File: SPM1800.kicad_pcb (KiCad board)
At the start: 2 copper layers, 314.3 x 83.3 mm, 140 parts, among them J1 Conn_01x02, J2 Conn_01x01, J3 Conn_01x03, U1 ATmega32U4-AU, Y1 Crystal_GND24_Small

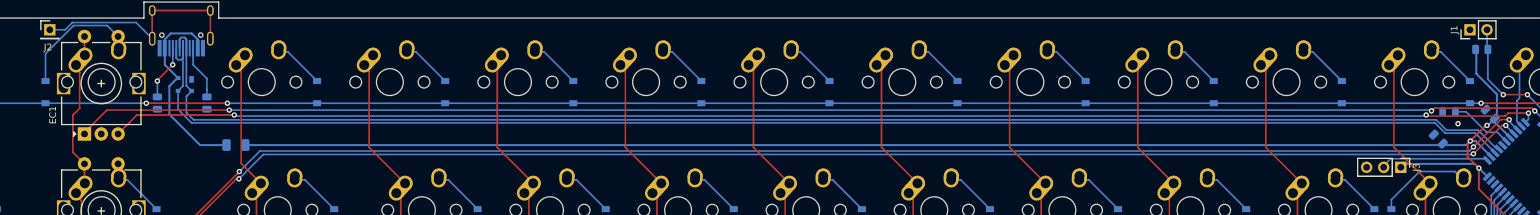
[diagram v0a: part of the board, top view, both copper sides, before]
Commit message: Updated PCB
Added series resistors to data lines.
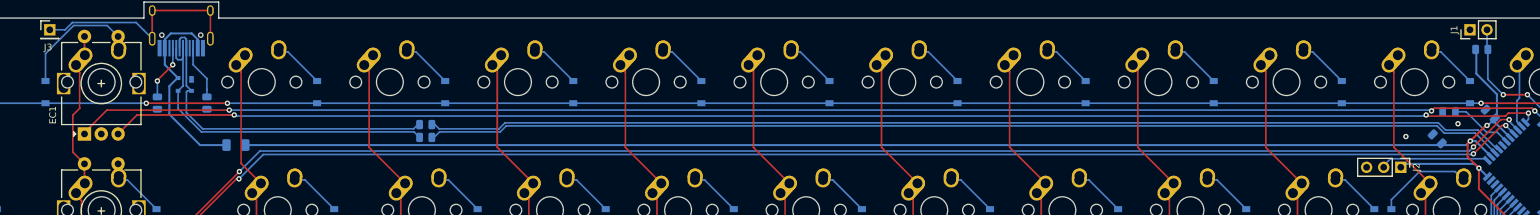
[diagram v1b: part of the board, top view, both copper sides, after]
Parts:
- added R5: 22, Resistor_SMD:R_0805_2012Metric, B.Cu at (187.1, -264.0)
- added R6: 22, Resistor_SMD:R_0805_2012Metric, B.Cu at (187.1, -265.9)
- R2: value R_Small -> 10k
- moved C5 0.17 mm to (337.5, -263.8)
- renumbered C8 to C1, C1 to C2, C2 to C3, C3 to C4, C4 to C5, C5 to C6, C6 to C7, C7 to C8, D56 to D55, D57 to D56, D58 to D57, D59 to D58, D60 to D59, J3 to J2, J2 to J3, MX56 to MX55, MX57 to MX56, MX58 to MX57, MX59 to MX58, MX60 to MX59, MX55 to MX60
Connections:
- D59 pad 2: D+ -> Net-(D59-Pad2)
- D59 pad 3: D- -> Net-(D59-Pad3)
- USB1 pad 5: D- -> Net-(D59-Pad3)
- USB1 pad 6: D+ -> Net-(D59-Pad2)
- USB1 pad 7: D- -> Net-(D59-Pad3)
- USB1 pad 8: D+ -> Net-(D59-Pad2)
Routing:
- net D-: track 212.1 -> 160.5 mm
- net Net-(D59-Pad3): track 0.00 -> 51.1 mm
- net D+: track 211.5 -> 160.8 mm
- net Net-(D59-Pad2): track 0.00 -> 50.4 mm
- net GND: vias 4 -> 5

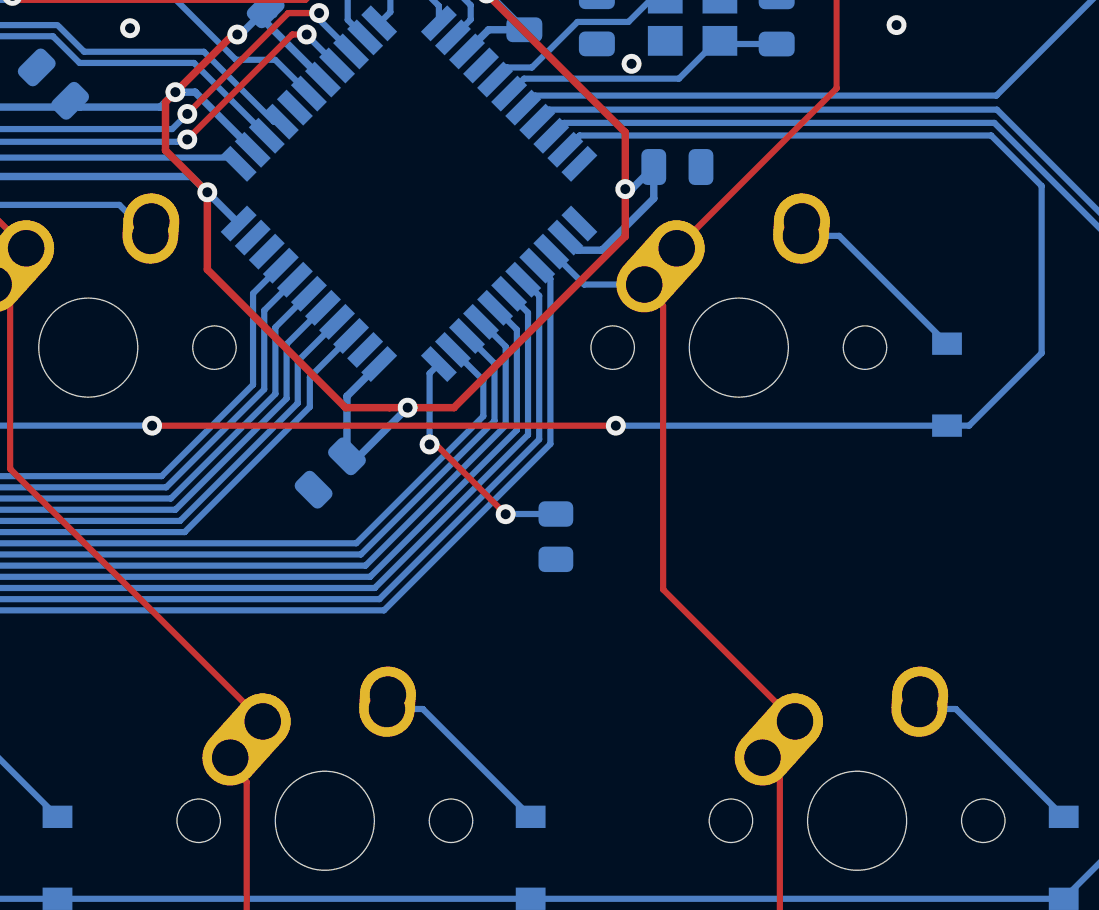
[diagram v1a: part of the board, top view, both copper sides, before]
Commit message: Updated PCB
COL13 to D4
COL15 to D5
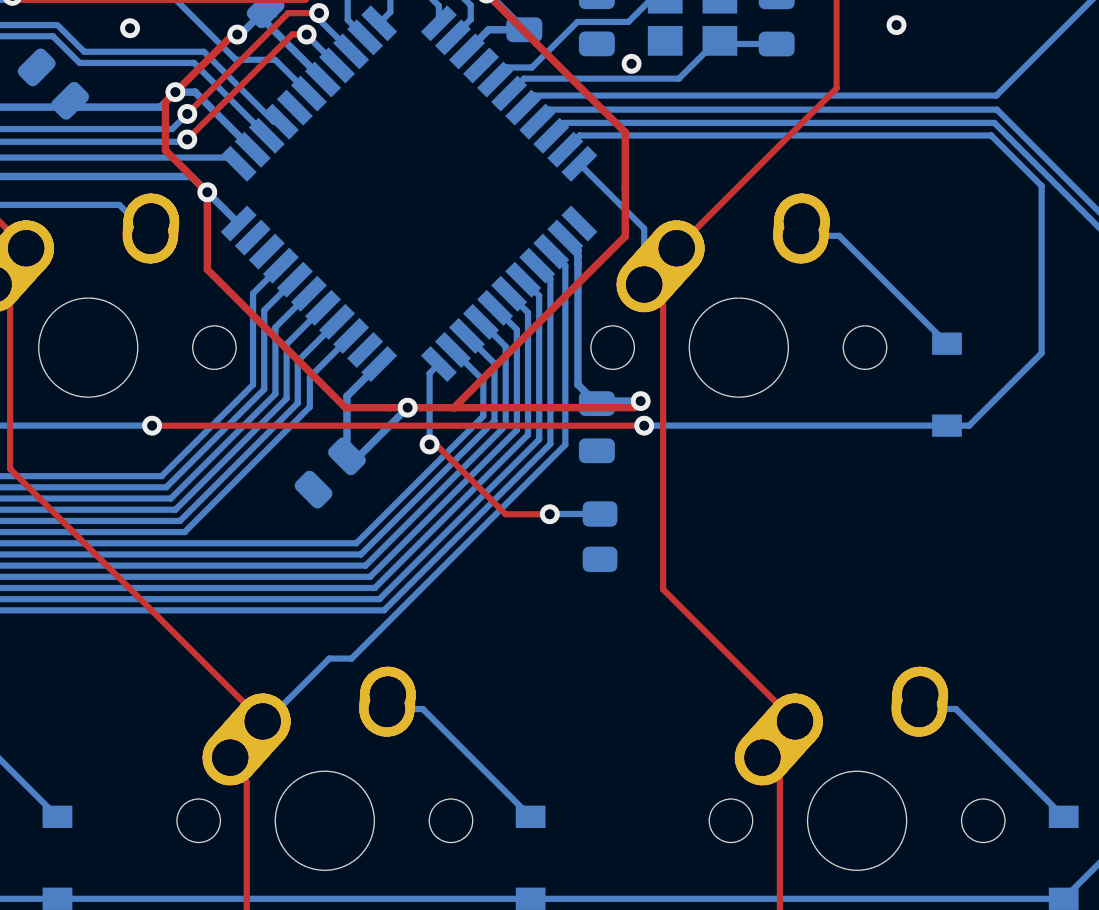
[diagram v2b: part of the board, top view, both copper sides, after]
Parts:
- moved C3 11.0 mm to (359.4, -250.0), turned to 270 degrees
- moved R2 1.78 mm to (359.5, -245.6)
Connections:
- U1 pad 22: Net-(U1-Pad22) -> COL15
- U1 pad 25: COL15 -> COL13
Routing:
- net COL13: track 60.3 -> 87.2 mm
- net +5V: track 283.0 -> 292.2 mm
- net Net-(R2-Pad2): track 9.65 -> 11.4 mm
- net COL15: track 63.0 -> 64.6 mm

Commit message: Updated Gerbers
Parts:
- moved C1 341.2 mm to (345.8, 74.0)
- moved C2 341.2 mm to (334.7, 73.5)
- moved C3 341.2 mm to (348.7, 91.0)
- moved C4 341.2 mm to (338.0, 92.8)
- moved C5 341.2 mm to (326.9, 77.2)
- moved C6 341.2 mm to (356.0, 74.6)
- moved C7 341.2 mm to (348.7, 74.6)
- moved C8 341.2 mm to (328.6, 73.2)
- moved D1 341.2 mm to (74.5, 70.2)
- moved D10 341.2 mm to (255.5, 70.2)
- moved D11 341.2 mm to (274.6, 70.2)
- moved D12 341.2 mm to (293.6, 70.2)
- moved D13 341.2 mm to (312.7, 70.2)
- moved D14 341.2 mm to (331.7, 70.2)
- moved D15 341.2 mm to (350.8, 70.2)
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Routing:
- net Net-(D3-Pad2): track 15.5 -> 7.55 mm

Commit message: Quick Fix
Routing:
- net ENC_S21: track 9.31 -> 10.1 mm

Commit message: Added kamelon pan
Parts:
- added G***: LOGO, silk:turtle_pan_cu_small, F.Cu at (144.2, 118.8)
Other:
- board text added: "MELONBRED - 2021.02"
- board text removed: "MELONBRED - 2020.11"
